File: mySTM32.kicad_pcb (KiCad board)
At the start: 2 copper layers, 138 x 118 mm, 118 parts, among them J1 conn1X2, J10 DB9_Female****, J11 USB_OTG, J12 conn2X16, J13 conn2X3, J14 Conn_02x02, J15 conn2X3, J16 conn1X2, J17 conn2X2, J18 JTAG, J19 Conn_02x17_Odd_Even, J2 USB_OTG, J20 Conn_02x22_Odd_Even, J21 conn2X9, J22 conn2X3, J23 Conn2x4, J3 conn2X3, J4 conn2X2, J5 conn2X2, J6 conn1X2, J7 Conn_01x02, J8 Conn2x4, J9 conn2X4, Q1 Q_NPN_BEC(S8050), Q2 Q_NPN_BEC, Q3 Q_NPN_BEC(S8050), SW1 KFT8.0, SW2 WAKUP, SW3 RESET, SW4 KE1, SW5 KEY2, U1 AT24C02, U2 W25Q16, U3 SD-Card, U4 SP3485, U5 SN65HVD230, U6 CH340G, U7 AMS1117, U8 SP3232, U9 STM32F103VET6, Y1 12MHz, Y2 32.768KHz, Y3 8MHz

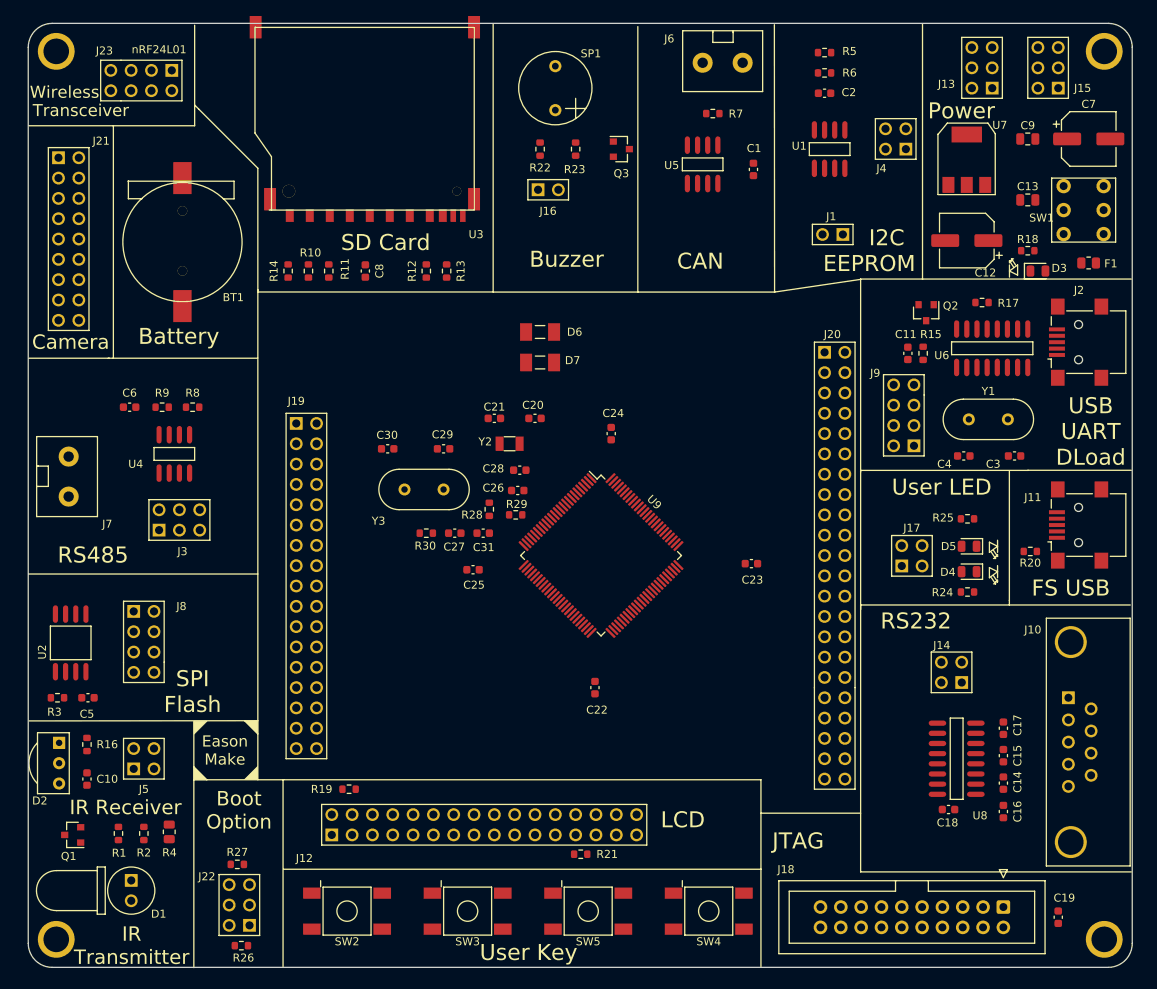
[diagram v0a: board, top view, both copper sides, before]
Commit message: [outline] change to 138*108mm [notes] notes on LED, Diode , IR, UserKey [align] left , right and LCD connector
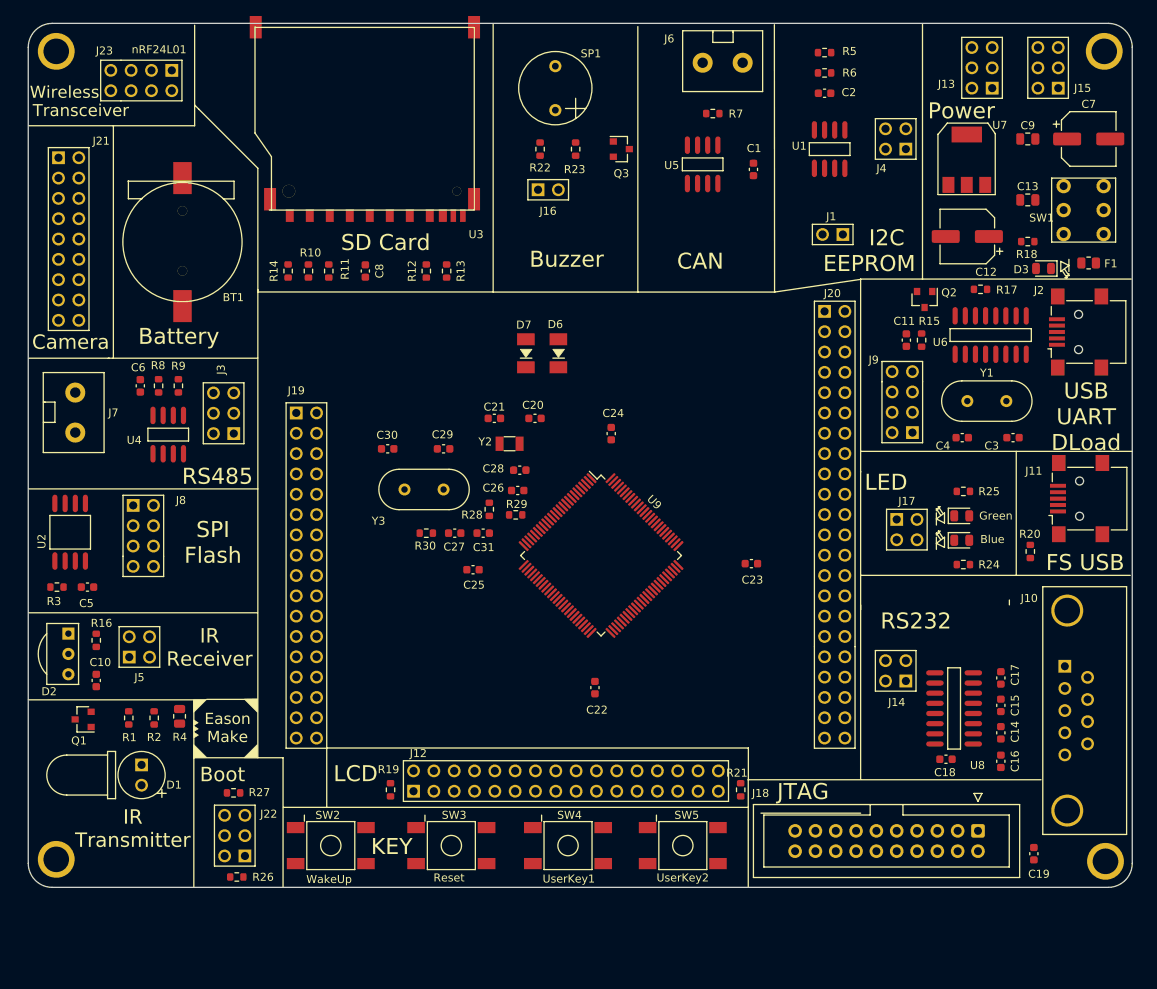
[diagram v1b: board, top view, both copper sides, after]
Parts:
- removed the REF** at (33.5, 144.5)
- removed the REF** at (164.5, 144.5)
- added REF**: KONG, mypcb:KONG, F.Cu at (33.5, 134.5)
- added REF**: KONG, mypcb:KONG, F.Cu at (164.7, 134.7)
- moved R21 21.6 mm to (119.1, 125.8), turned to 270 degrees
- moved SW4 19.4 mm to (97.5, 132.8)
- moved R1 14.5 mm to (42.6, 116.8)
- moved R2 14.5 mm to (45.7, 116.8)
- moved D1 14.5 mm to (44.2, 124.0)
- moved Q1 14.5 mm to (36.9, 117.0)
- moved R4 14.5 mm to (48.9, 116.6)
- moved SW5 14.4 mm to (111.8, 132.8)
- moved J5 14.0 mm to (42.6, 107.9)
- moved C5 13.8 mm to (37.4, 100.5)
- moved R3 13.8 mm to (33.6, 100.5)
- moved U2 13.8 mm to (35.2, 93.6)
- moved D2 13.7 mm to (35.0, 108.8)
- moved J3 13.5 mm to (54.4, 81.3), turned to 90 degrees
- moved J8 13.2 mm to (44.4, 90.3)
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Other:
- board size 138 x 118 mm -> 138 x 108 mm
- board text added: "Blue"
- board text added: "Boot"
- board text added: "Green"
- board text added: "KEY"
- board text added: "LED"
- board text added: "Reset"
- board text added: "UserKey1"
- board text added: "UserKey2"
- board text added: "WakeUp"
- board text removed: "Boot Option"
- board text removed: "User Key"
- board text removed: "User LED"

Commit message: [assembly] LCD connector [other]	re-Layout
Signed-off-by: EasonLiang <liangyx25@163.com>
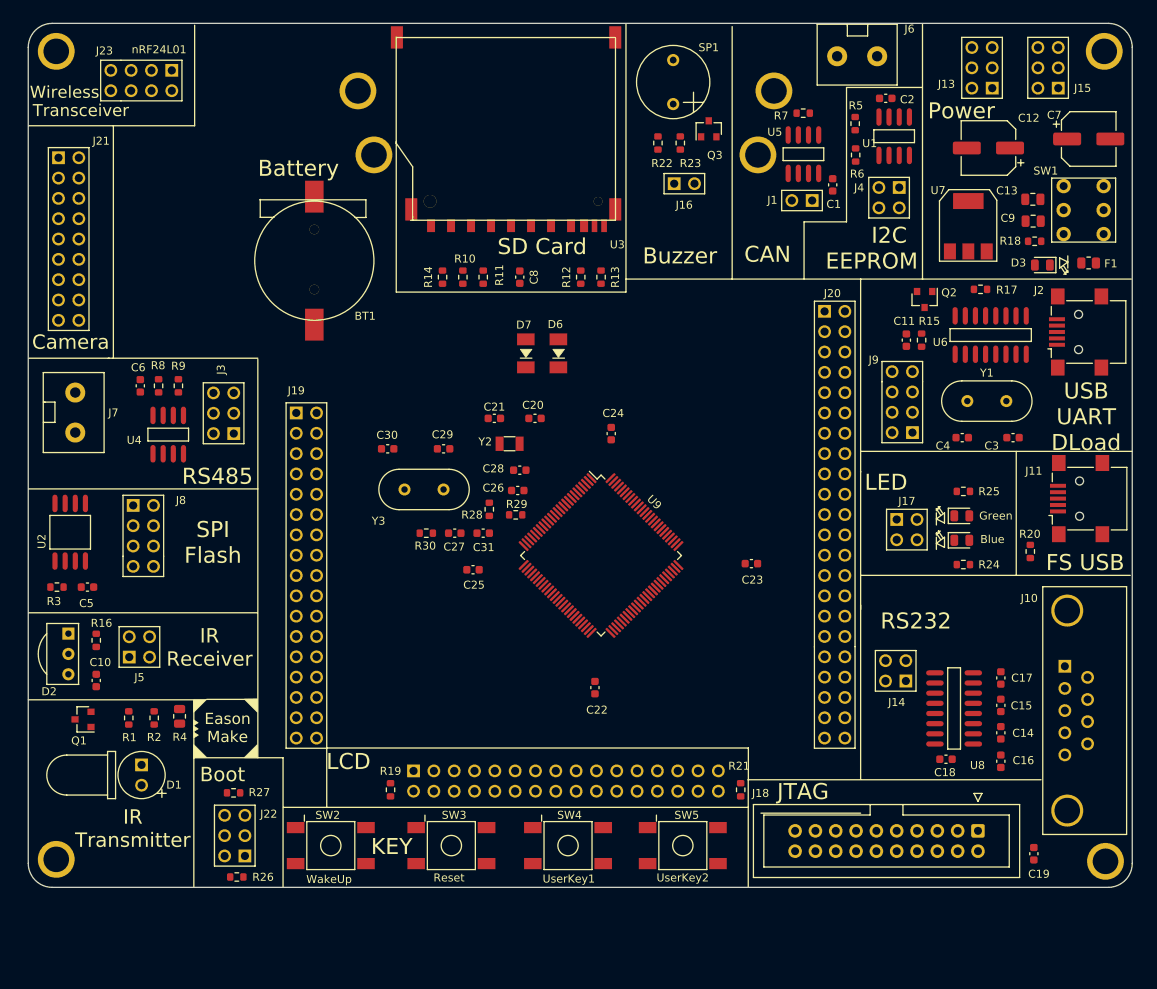
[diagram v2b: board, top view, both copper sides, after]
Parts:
- added REF**: KONG, mypcb:KONG, F.Cu at (69.8, 33.7)
- added REF**: KONG, mypcb:KONG, F.Cu at (108.1, 32.8)
- added REF**: KONG, mypcb:KONG, F.Cu at (107.6, 41.0)
- added REF**: KONG, mypcb:KONG, F.Cu at (78.1, 42.3)
- J12: moved to B.Cu
- moved C8 19.3 mm to (91.4, 61.7)
- moved R10 19.3 mm to (84.3, 61.7)
- moved R11 19.3 mm to (86.9, 61.7)
- moved R12 19.3 mm to (99.1, 61.7)
- moved R14 19.3 mm to (81.8, 61.7)
- moved R13 19.3 mm to (101.6, 61.7)
- moved U3 17.7 mm to (103.4, 31.8)
- moved J16 17.0 mm to (112.0, 50.0)
- moved J6 16.8 mm to (131.1, 34.1)
- moved BT1 16.6 mm to (65.8, 59.7)
- moved R22 14.8 mm to (108.7, 45.0)
- moved SP1 14.8 mm to (110.6, 37.3)
- moved R23 13.1 mm to (111.5, 45.0)
- moved U5 12.7 mm to (126.9, 46.4)
- moved C12 11.4 mm to (150.0, 45.6)
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
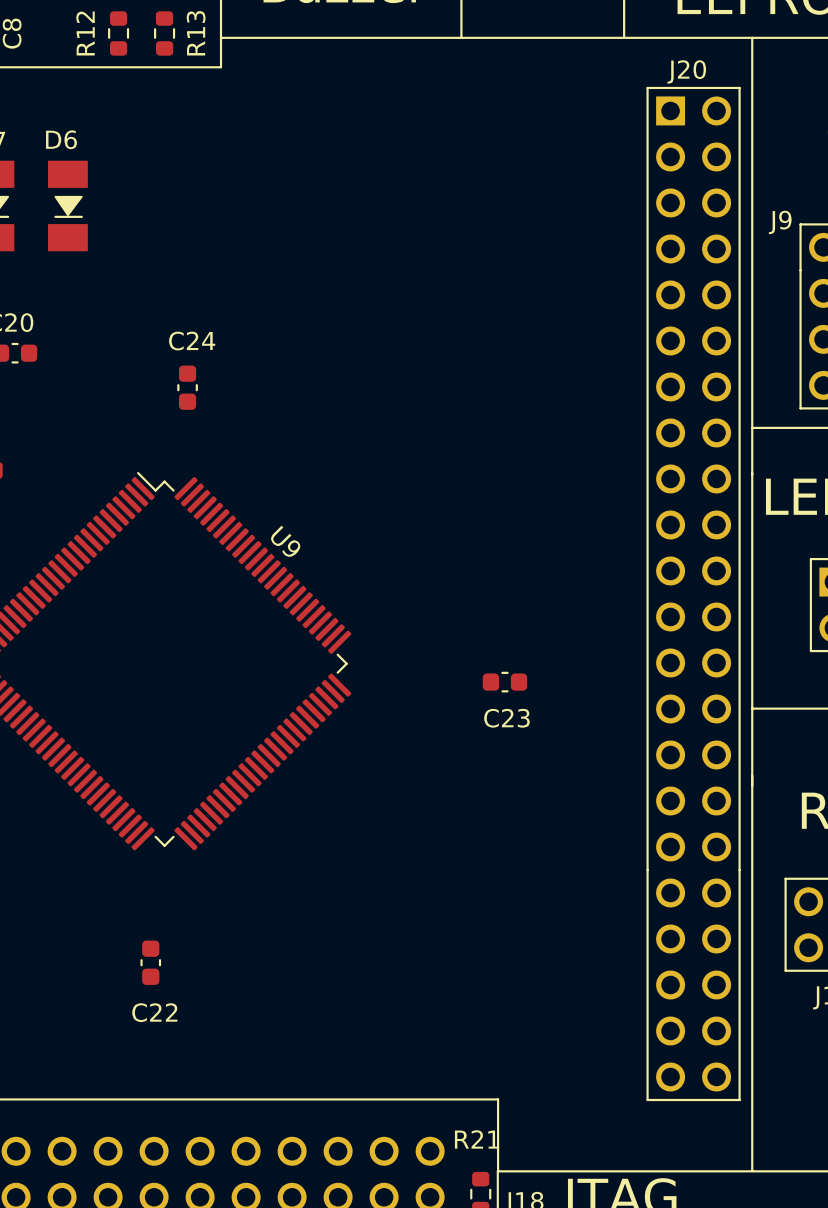
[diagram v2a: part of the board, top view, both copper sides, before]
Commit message: [right connector] [trace width] to 10mil
Signed-off-by: EasonLiang <liangyx25@163.com>
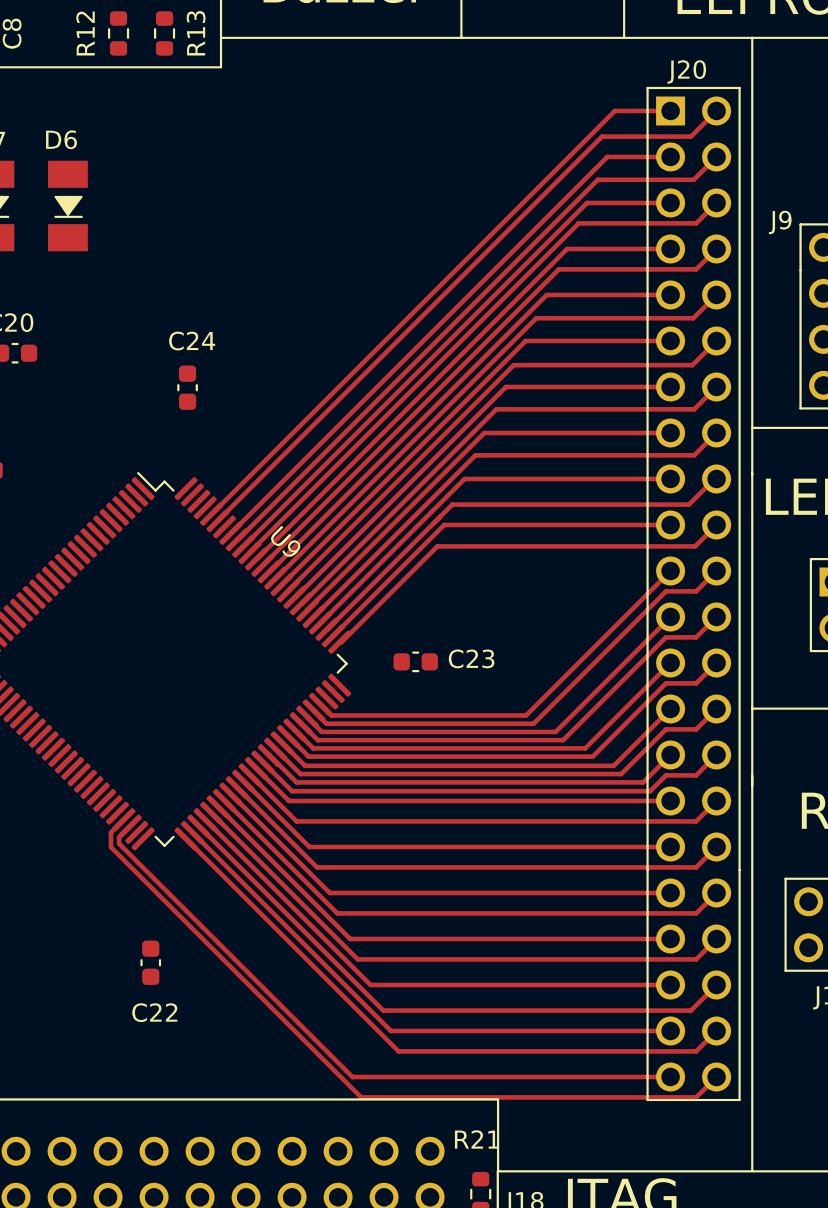
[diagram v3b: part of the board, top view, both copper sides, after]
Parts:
- moved C23 5.05 mm to (115.5, 96.4)
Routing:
- net /PB10: track 0.00 -> 41.4 mm
- net /PB11: track 0.00 -> 37.0 mm
- net /CAN_RX: track 0.00 -> 36.9 mm
- net /I2C1_SCL: track 0.00 -> 35.2 mm
- net /PB12: track 0.00 -> 34.6 mm
- net /CAN_TX: track 0.00 -> 34.6 mm
- net /NJTRST: track 0.00 -> 33.8 mm
- net /PB14: track 0.00 -> 33.4 mm
- net /I2C1_SDA: track 0.00 -> 32.9 mm
- net /FSMC_NE1: track 0.00 -> 32.3 mm
- net /DB13: track 0.00 -> 31.7 mm
- net /LED1: track 0.00 -> 31.4 mm
- net /PB13: track 0.00 -> 30.9 mm
- net /FSMC_NWE: track 0.00 -> 30.8 mm
- net /DB15: track 0.00 -> 30.2 mm
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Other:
- net class Default: trace_width 0.25 -> 0.254

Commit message: [left connector] [crystal]
Signed-off-by: EasonLiang <liangyx25@163.com>
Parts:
- moved C28 17.2 mm to (106.4, 77.5), turned to 270 degrees
- moved C30 12.6 mm to (85.9, 77.0), turned to 45 degrees
- moved R30 11.2 mm to (88.4, 86.6), turned to 180 degrees
- moved C24 8.10 mm to (109.7, 77.0)
- moved C31 8.07 mm to (83.1, 86.6)
- moved Y3 7.04 mm to (86.4, 82.8), turned to 45 degrees
- moved R28 6.19 mm to (81.5, 91.9), turned to 180 degrees
- moved R29 5.86 mm to (85.1, 91.9)
- moved C27 5.65 mm to (88.6, 91.9)
- moved C21 5.46 mm to (93.7, 79.2), turned to 270 degrees
- moved Y2 4.07 mm to (94.2, 82.8)
- moved C26 3.66 mm to (93.2, 85.3), turned to 180 degrees
- moved C29 3.30 mm to (82.8, 80.0), turned to 45 degrees
- moved D6 2.92 mm to (96.4, 68.3)
- moved C20 2.67 mm to (96.0, 79.2), turned to 270 degrees
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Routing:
- net /OV_PE6: track 0.00 -> 51.8 mm
- net /NRF_CSN: track 0.00 -> 50.1 mm
- net /OV_PE4: track 0.00 -> 50.0 mm
- net /OV_PE3: track 0.00 -> 47.0 mm
- net /OV_PE5: track 0.00 -> 46.9 mm
- net /DB11: track 0.00 -> 41.3 mm
- net /DB7: track 0.00 -> 40.2 mm
- net /DB9: track 0.00 -> 39.9 mm
- net /DB12: track 0.00 -> 39.0 mm
- net /DB8: track 0.00 -> 38.1 mm
- net /DB10: track 0.00 -> 37.5 mm
- net /DB5: track 0.00 -> 36.9 mm
- net /BOOT1: track 0.00 -> 35.5 mm
- net /DB6: track 0.00 -> 34.6 mm
- net /KEY1: track 0.00 -> 34.5 mm, vias 0 -> 1
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
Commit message: [power]
Signed-off-by: EasonLiang <liangyx25@163.com>
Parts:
- moved C13 11.6 mm to (144.5, 48.6), turned to 180 degrees
- moved R18 8.35 mm to (148.2, 60.7)
- moved D3 4.07 mm to (152.7, 60.6)
- moved J13 1.42 mm to (148.6, 36.8)
- moved J15 1.21 mm to (157.4, 36.9)
- moved C9 1.11 mm to (154.5, 54.8), turned to 270 degrees
- moved SW1 0.76 mm to (162.7, 53.3)
- moved F1 0.63 mm to (161.9, 59.9), turned to 180 degrees
- moved U7 0.48 mm to (147.3, 54.9)
- turned C12 to 0 degrees
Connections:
- C7 pad 1: Net-(C7-Pad1) -> /5V
- C9 pad 1: Net-(C7-Pad1) -> /5V
- J15 pad 2: +5V -> /5V
- J15 pad 4: +5V -> /5V
- J15 pad 6: +5V -> /5V
- SW1 pad 2: Net-(C7-Pad1) -> /5V
- SW1 pad 5: Net-(C7-Pad1) -> /5V
- U7 pad 3: Net-(C7-Pad1) -> /5V
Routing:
- net /5V: track 0.00 -> 49.6 mm
- net GND: track 6.03 -> 41.4 mm
- net +3V3: track 6.91 -> 38.7 mm
- net +5V: track 0.00 -> 12.6 mm
- net Net-(F1-Pad2): track 0.00 -> 12.0 mm
- net Net-(D3-Pad2): track 0.00 -> 2.77 mm
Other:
- board text added: "3.3"
- board text added: "5"
- board text added: "GND"

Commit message: [usb2uart, uart download]
Signed-off-by: EasonLiang <liangyx25@163.com>
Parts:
- moved C4 11.3 mm to (155.6, 74.7), turned to 180 degrees
- moved R17 9.41 mm to (141.0, 68.1), turned to 90 degrees
- moved Y1 9.12 mm to (156.1, 80.0), turned to 180 degrees
- moved R15 8.48 mm to (147.6, 63.5), turned to 180 degrees
- moved C3 7.13 mm to (152.5, 74.7), turned to 0 degrees
- moved C11 4.13 mm to (143.6, 68.0)
- moved J9 3.38 mm to (142.5, 81.9)
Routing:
- net /PA9: track 23.1 -> 43.5 mm
- net /PA10: track 26.1 -> 44.5 mm
- net /CH340_DTR: track 0.00 -> 14.3 mm
- net +3V3: track 38.7 -> 52.2 mm, vias 0 -> 2
- net /CH340_RXD: track 0.00 -> 12.5 mm
- net /BOOT0_CTR: track 0.00 -> 11.1 mm
- net Net-(C3-Pad2): track 0.00 -> 9.63 mm
- net Net-(J2-Pad3): track 0.00 -> 9.60 mm
- net /CH340_TXD: track 0.00 -> 9.39 mm
- net Net-(C4-Pad2): track 0.00 -> 9.22 mm
- net Net-(J2-Pad2): track 0.00 -> 8.06 mm
- net GND: track 41.4 -> 48.4 mm
- net Net-(Q2-Pad1): track 0.00 -> 3.75 mm
- net Net-(R15-Pad1): track 0.00 -> 3.50 mm

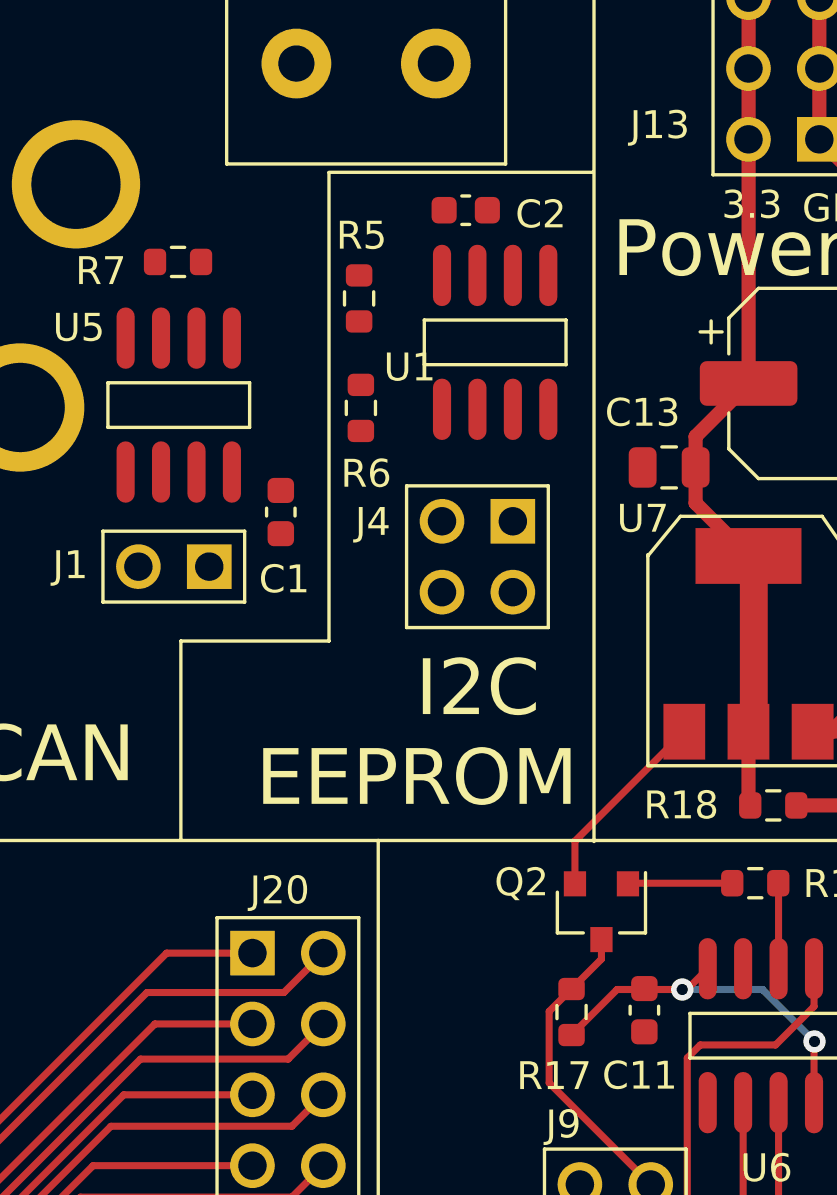
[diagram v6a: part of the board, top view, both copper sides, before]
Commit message: [I2C EEPROM] [schematic validation on I2C ]
Signed-off-by: EasonLiang <liangyx25@163.com>
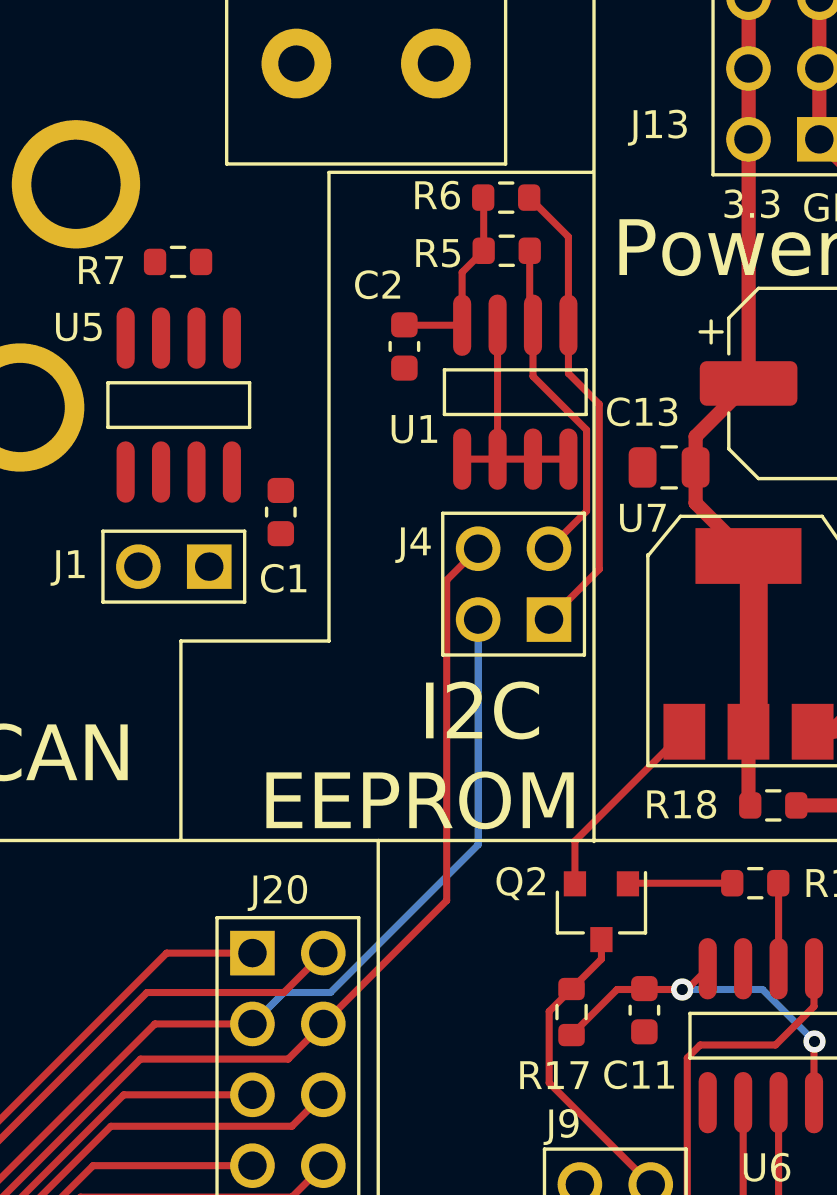
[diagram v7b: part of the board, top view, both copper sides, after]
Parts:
- moved R6 9.16 mm to (138.6, 38.9), turned to 180 degrees
- moved R5 5.56 mm to (138.7, 40.8), turned to 180 degrees
- moved C2 5.36 mm to (135.0, 44.3), turned to 90 degrees
- moved J4 2.25 mm to (138.9, 54.0), turned to 90 degrees
- moved U1 1.93 mm to (139.0, 45.9)
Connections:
- R5 pad 1: Net-(J4-Pad1) -> Net-(J4-Pad3)
- U1 pad 5: Net-(J4-Pad3) -> Net-(J4-Pad1)
- U1 pad 6: Net-(J4-Pad1) -> Net-(J4-Pad3)
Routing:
- net /I2C1_SCL: track 35.2 -> 54.6 mm
- net /I2C1_SDA: track 32.9 -> 51.7 mm
- net Net-(J4-Pad1): track 0.00 -> 16.9 mm
- net Net-(J4-Pad3): track 0.00 -> 12.1 mm
- net GND: track 48.4 -> 57.1 mm
- net +3V3: track 52.2 -> 59.2 mm
